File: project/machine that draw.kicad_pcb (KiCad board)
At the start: 2 copper layers, 23 parts, among them J1 SD_Card, J2 SSD1306 / 1 GND / 2 VCC / 3 S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, J3 limit switch_X, J4 limit switch_Y, J5 Motor_X, J6 motor_Y, J7 Barrel_Jack, J8 Conn_02x03_Odd_Even, J9 Conn_02x03_Odd_Even, U1 ESP32-S3-UNO, U2 Regulateur

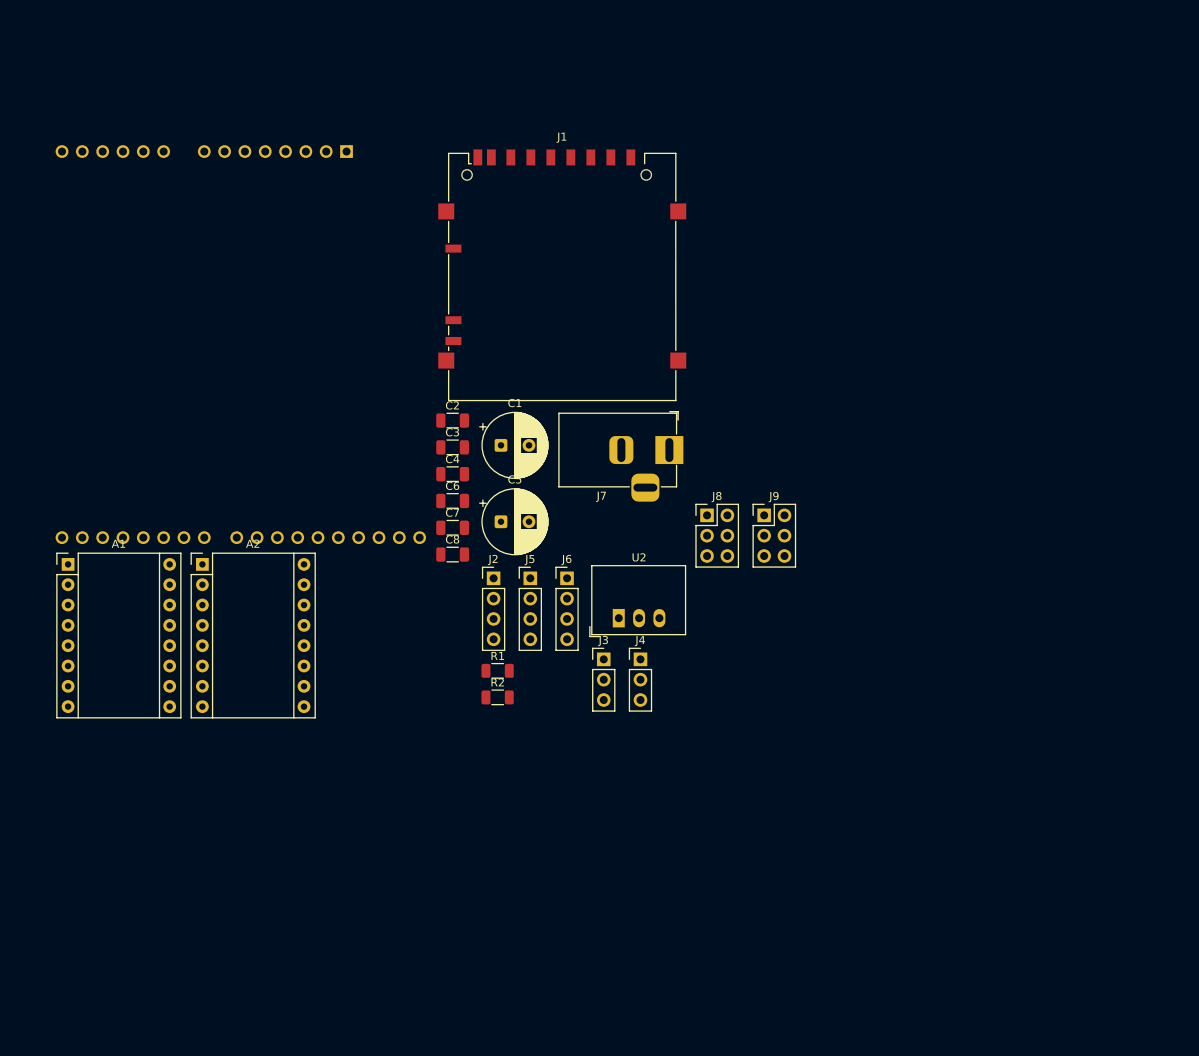
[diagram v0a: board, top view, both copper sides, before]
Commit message: PCB composant placed
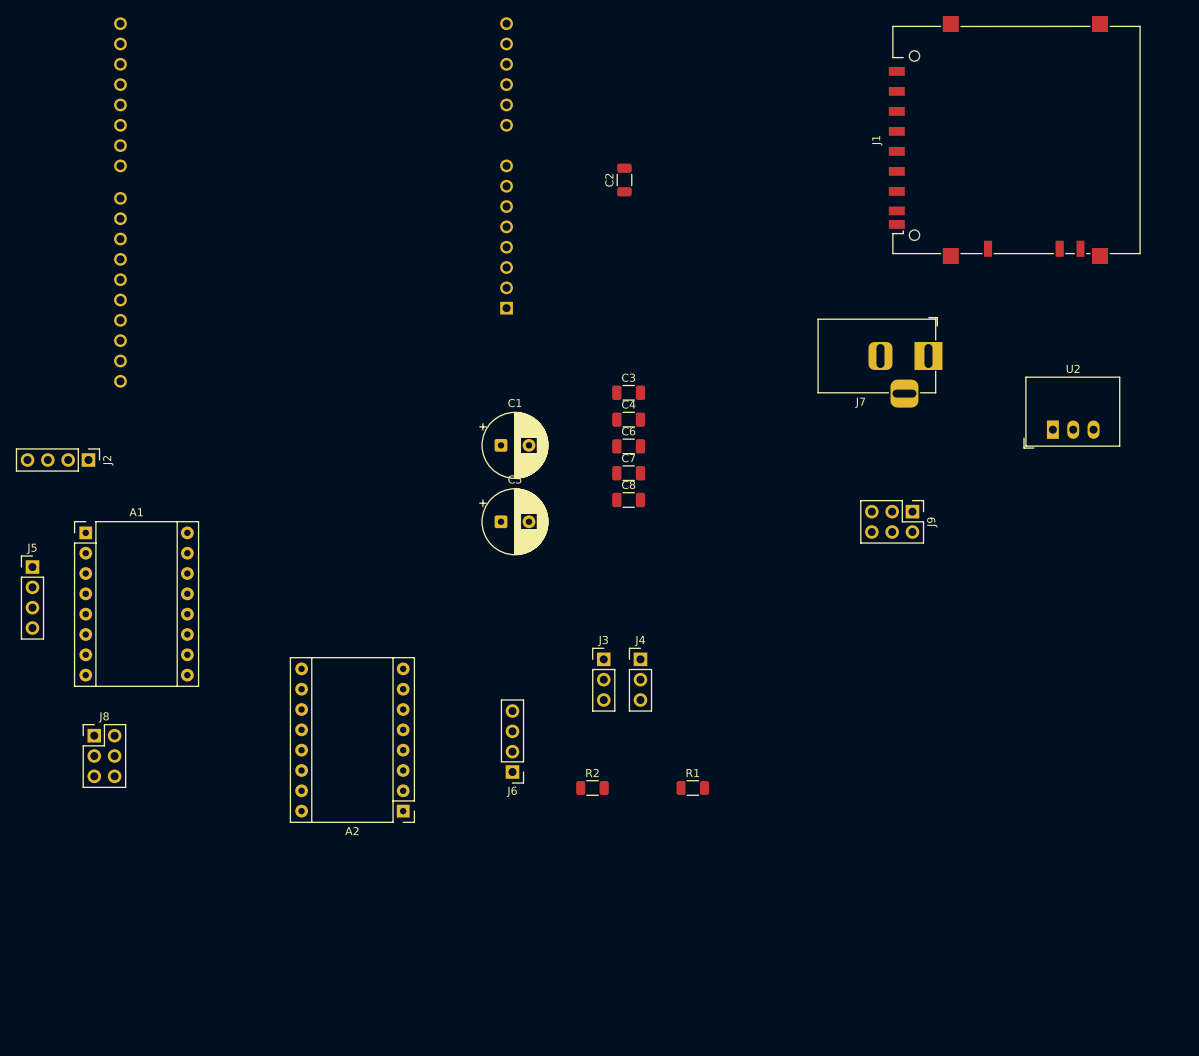
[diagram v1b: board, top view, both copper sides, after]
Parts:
- moved J8 81.4 mm to (37.7, 106.5)
- moved J5 62.2 mm to (30.0, 85.4)
- moved J1 59.3 mm to (153.0, 32.0), turned to 90 degrees
- moved U2 59.2 mm to (157.6, 68.2)
- moved J2 52.8 mm to (37.0, 72.0), turned to -90 degrees
- moved A2 39.8 mm to (76.3, 115.9), turned to 180 degrees
- moved C2 37.0 mm to (104.0, 37.0), turned to 90 degrees
- moved J7 34.5 mm to (142.0, 59.0)
- moved R1 28.4 mm to (112.5, 113.0)
- moved U1 28.0 mm to (89.3, 53.0), turned to -90 degrees
- moved J6 25.2 mm to (90.0, 111.0), turned to 180 degrees
- moved C3 23.0 mm to (104.5, 63.6)
- moved C6 23.0 mm to (104.5, 70.3)
- moved C4 23.0 mm to (104.5, 67.0)
- moved C7 23.0 mm to (104.5, 73.7)
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
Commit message: EDITED PCB
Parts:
- moved J9 84.3 mm to (57.0, 64.0), turned to 180 degrees
- moved A2 67.2 mm to (68.7, 49.1), turned to 0 degrees
- moved J6 62.1 mm to (65.0, 54.2), turned to 0 degrees
- moved J1 59.7 mm to (115.5, 78.5)
- moved J8 57.5 mm to (77.5, 65.0), turned to 180 degrees
- moved J2 56.1 mm to (93.0, 74.4), turned to 0 degrees
- moved U2 49.8 mm to (109.0, 57.0), turned to 90 degrees
- moved C6 39.5 mm to (67.5, 84.0)
- moved R1 39.4 mm to (89.0, 81.5), turned to 90 degrees
- moved C5 39.0 mm to (49.6, 79.7), turned to -90 degrees
- moved C4 38.5 mm to (68.0, 79.0)
- moved J4 35.6 mm to (74.9, 79.6), turned to 90 degrees
- moved R2 35.0 mm to (84.9, 81.5), turned to 90 degrees
- moved A1 33.8 mm to (47.7, 49.1)
- moved J5 33.8 mm to (41.0, 53.4)
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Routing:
- net GND: track 0.00 -> 266.8 mm, vias 0 -> 2
- net +12V: track 0.00 -> 115.8 mm
- net +3V3: track 0.00 -> 98.1 mm, vias 0 -> 2
- net MISO: track 0.00 -> 96.5 mm, vias 0 -> 1
- net +5V: track 0.00 -> 94.1 mm, vias 0 -> 3
- net SCK: track 0.00 -> 90.2 mm, vias 0 -> 2
- net MOSI: track 0.00 -> 81.1 mm, vias 0 -> 1
- net CS: track 0.00 -> 73.9 mm, vias 0 -> 1
- net STEP_X: track 0.00 -> 60.3 mm, vias 0 -> 1
- net LIMIT_X: track 0.00 -> 59.9 mm, vias 0 -> 1
- net DIR_X: track 0.00 -> 55.1 mm, vias 0 -> 1
- net LIMIT_Y: track 0.00 -> 53.3 mm, vias 0 -> 1
- net ENA: track 0.00 -> 52.1 mm
- net DIR_Y: track 0.00 -> 48.8 mm
- net STEP_Y: track 0.00 -> 47.7 mm
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
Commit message: finalisation pcb
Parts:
- removed C8: 10uF, makerspace-unilasalle:C_1206
- added C9: 10 uF, Capacitor_SMD:C_1206_3216Metric_Pad1.33x1.80mm_HandSolder, F.Cu at (122.9, 87.4)
- added F1: Fuse, Fuse:Fuseholder_Blade_Mini_Keystone_3568, F.Cu at (155.3, 130.4)
- added J10: Screw_Terminal_01x02, TerminalBlock_Phoenix:TerminalBlock_Phoenix_MKDS-1,5-2_1x02_P5.00mm_Horizontal, F.Cu at (166.5, 120.4)
- C4: footprint makerspace-unilasalle:C_1206 -> Capacitor_SMD:C_1206_3216Metric_Pad1.33x1.80mm_HandSolder
- C7: value 100nF -> 10 uF; footprint makerspace-unilasalle:C_1206 -> Capacitor_SMD:C_1206_3216Metric_Pad1.33x1.80mm_HandSolder
- moved C4 99.1 mm to (164.6, 101.1), turned to 180 degrees
- moved C1 95.2 mm to (152.4, 98.0), turned to 0 degrees
- moved C3 94.2 mm to (170.4, 113.8), turned to 90 degrees
- moved J4 92.5 mm to (165.5, 98.0), turned to -90 degrees
- moved J5 90.6 mm to (128.0, 78.7)
- moved J7 89.0 mm to (166.0, 130.6), turned to 90 degrees
- moved A1 87.5 mm to (131.7, 73.6)
- moved A2 87.0 mm to (152.2, 73.6)
- moved J6 86.9 mm to (148.4, 78.7)
- moved C2 86.5 mm to (170.4, 106.6), turned to 90 degrees
- moved C5 84.0 mm to (131.5, 98.0), turned to 0 degrees
- moved J9 83.8 mm to (138.4, 83.8), turned to 0 degrees
- moved J8 83.5 mm to (158.9, 83.8), turned to 0 degrees
- moved R2 81.4 mm to (163.3, 59.1), turned to 0 degrees
- moved U2 79.9 mm to (166.3, 112.7)
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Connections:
- C4 pad 2: Net-(J4-Pin_1) -> GND
- C6 pad 2: Net-(J3-Pin_1) -> GND
- J3 pad 1: Net-(J3-Pin_1) -> +5V
- J4 pad 1: Net-(J4-Pin_1) -> +5V
- J7 pad 1: +12V -> Net-(F1-Pad1)
- J8 pad 2: Net-(A2-MS1) -> Net-(A2-MS3)
- J8 pad 6: Net-(A2-MS3) -> Net-(A2-MS1)
- J9 pad 2: Net-(A1-MS1) -> Net-(A1-MS3)
- J9 pad 6: Net-(A1-MS3) -> Net-(A1-MS1)
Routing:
- net GND: track 266.8 -> 0.00 mm, vias 2 -> 0
- net MISO: track 96.5 -> 8.95 mm, vias 1 -> 0
- net SCK: track 90.2 -> 16.1 mm, vias 2 -> 0
- net MOSI: track 81.1 -> 24.6 mm, vias 1 -> 0
- net CS: track 73.9 -> 26.5 mm, vias 1 -> 0
- net +12V: track 115.8 -> 69.7 mm
- net DIR_Y: track 48.8 -> 6.25 mm
- net STEP_Y: track 47.7 -> 6.25 mm
- net LIMIT_X: track 59.9 -> 20.0 mm
- net STEP_X: track 60.3 -> 28.8 mm, vias 1 -> 0
- net DIR_X: track 55.1 -> 28.8 mm, vias 1 -> 0
- net SCL: track 25.0 -> 9.95 mm
- net Net-(J10-Pin_2): track 0.00 -> 13.2 mm
- net LIMIT_Y: track 53.3 -> 42.0 mm, vias 1 -> 0
- net SDA: track 18.7 -> 7.92 mm
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- added copper zone on B.Cu, net GND
- added copper zone on F.Cu, net GND
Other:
- board outline added: 53.1 x 84.4 mm

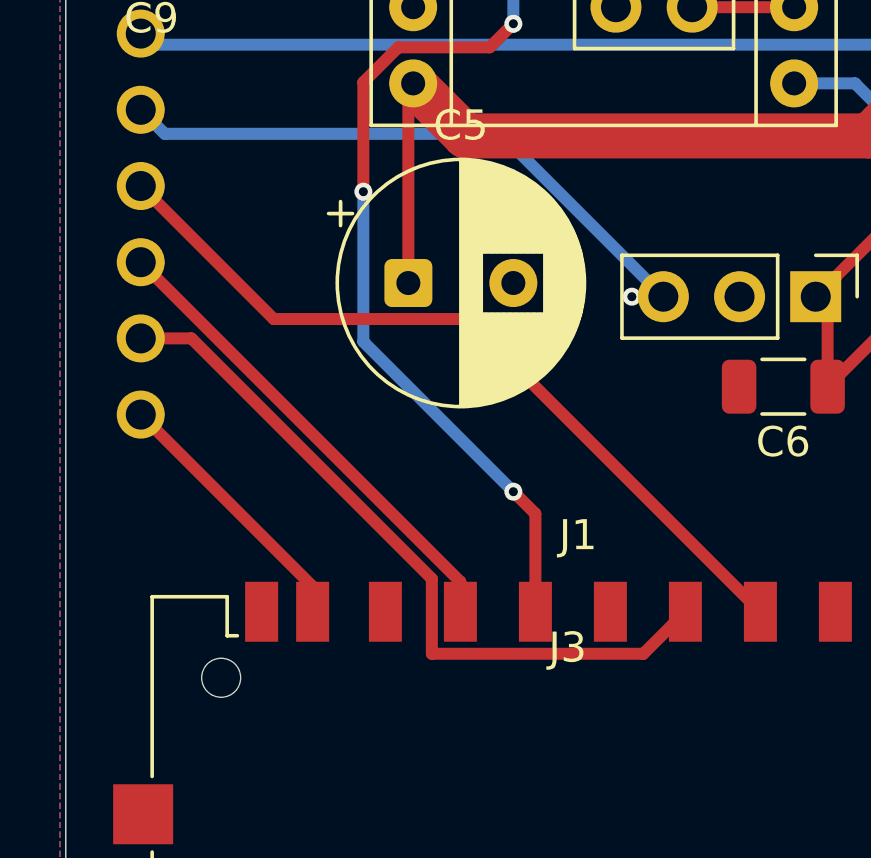
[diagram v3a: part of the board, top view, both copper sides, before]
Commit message: Validation PCB pour production
Nota : re-génération de plan de masse
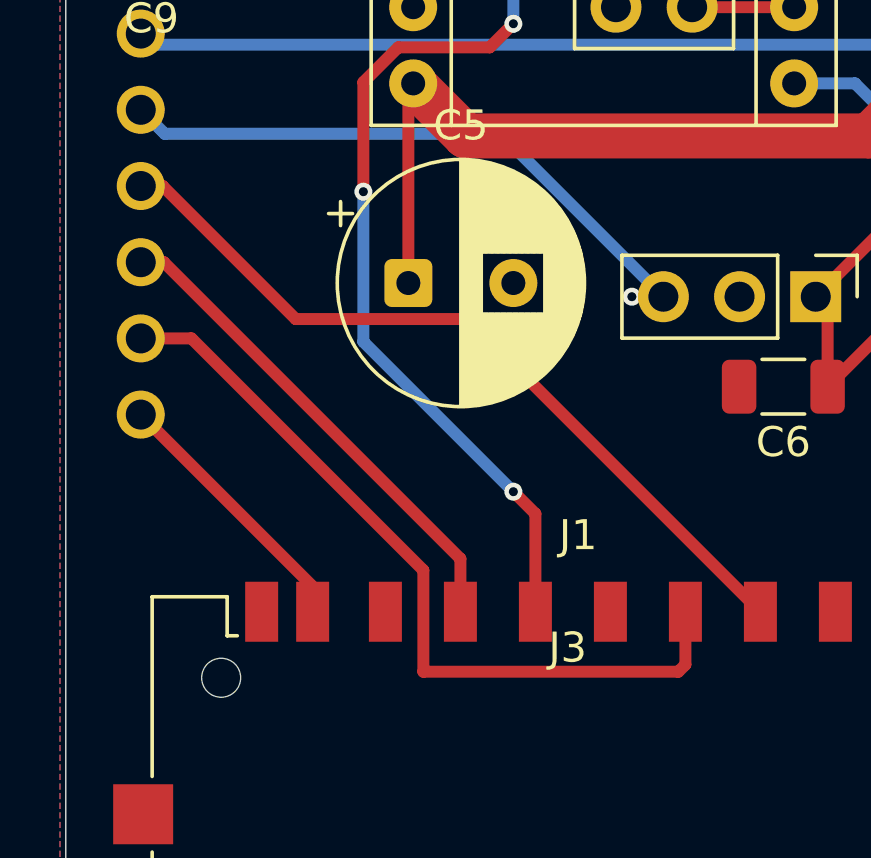
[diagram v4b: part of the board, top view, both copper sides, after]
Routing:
- net MOSI: track 24.6 -> 26.6 mm

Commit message: fix wiring problems
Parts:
- moved C9 22.1 mm to (143.5, 95.5), turned to 0 degrees
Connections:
- J7 pad 1: Net-(F1-Pad1) -> +12V
- U1 pad 25: STEP_Y -> DIR_Y
- U1 pad 26: DIR_Y -> STEP_Y
- U1 pad 8: +5V -> +12V
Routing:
- net +5V: track 88.9 -> 58.0 mm
- net +12V: track 69.7 -> 88.2 mm
- net STEP_Y: track 6.25 -> 11.2 mm
- net MOSI: track 26.6 -> 27.8 mm
- net DIR_Y: track 6.25 -> 6.77 mm
